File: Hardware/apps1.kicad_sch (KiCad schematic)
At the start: 12 parts, among them U114 TLV9152IDDFR

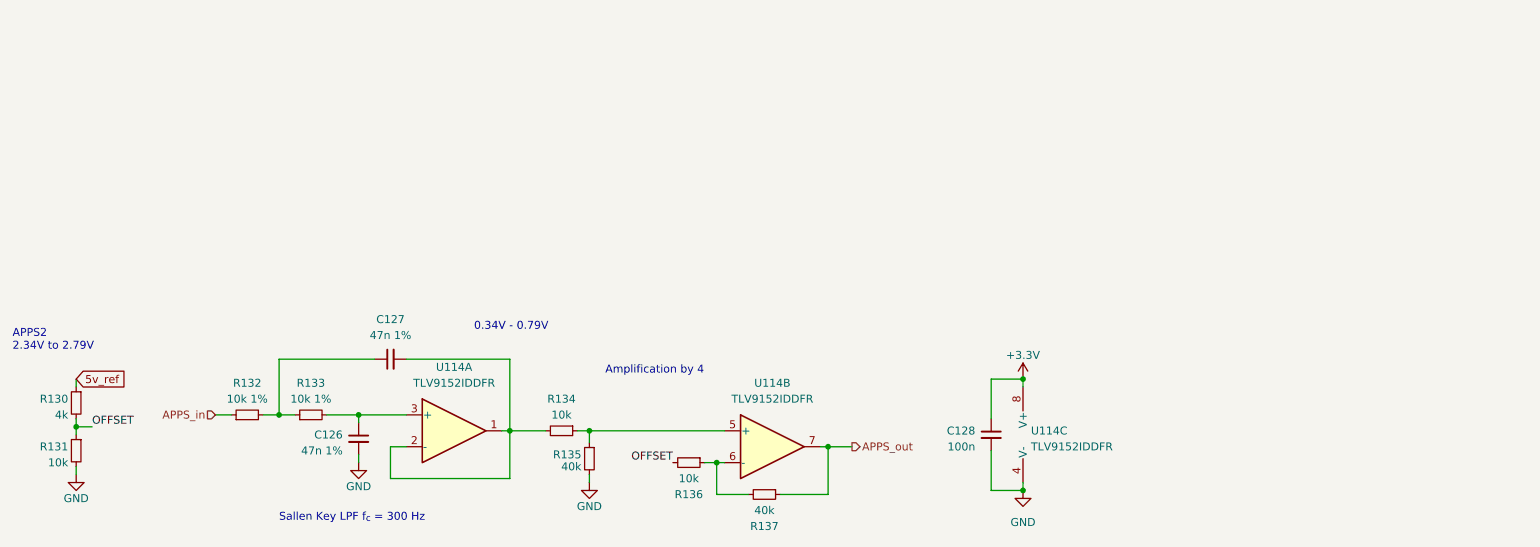
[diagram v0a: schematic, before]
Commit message: Changes in current layout, added tensometers to layout
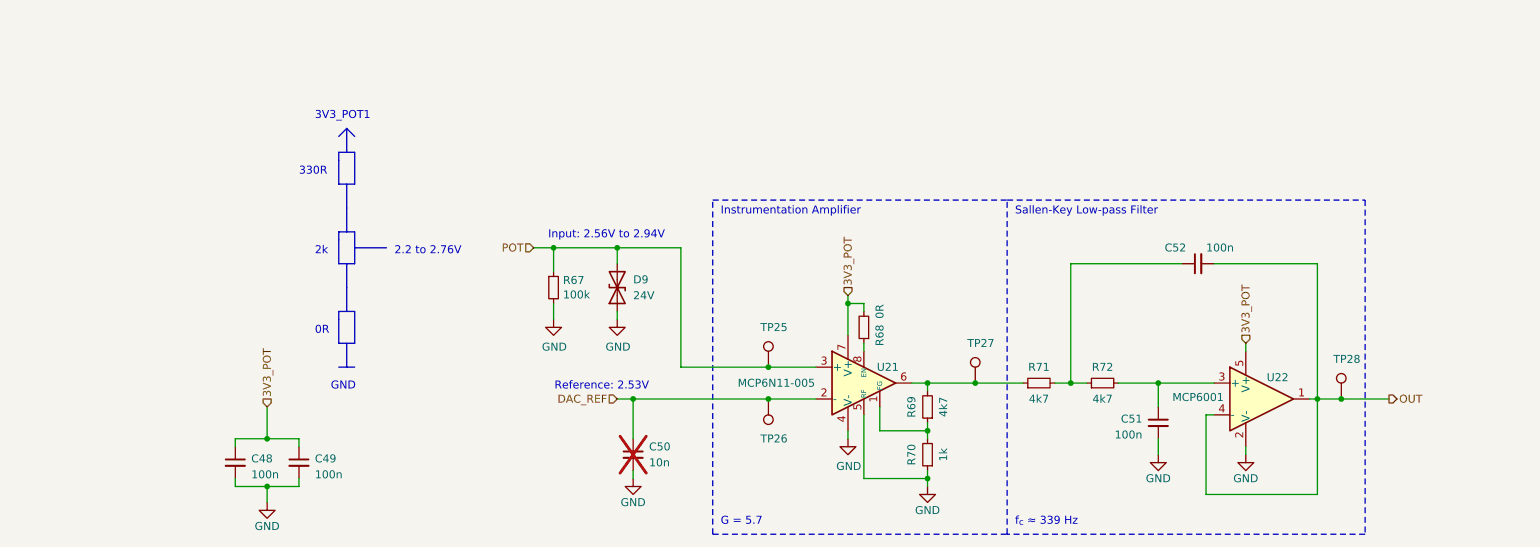
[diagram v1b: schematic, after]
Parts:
- removed C126, C127: 47n 1%, Capacitor_SMD:C_0402_1005Metric_Pad0.74x0.62mm_HandSolder, symbol Device:C_Small
- removed C128: 100n, Capacitor_SMD:C_0402_1005Metric_Pad0.74x0.62mm_HandSolder, symbol Device:C_Small
- removed R130: 4k, Resistor_SMD:R_0402_1005Metric, symbol Device:R_Small
- removed R131, R134, R136: 10k, Resistor_SMD:R_0402_1005Metric, symbol Device:R_Small
- removed R132, R133: 10k 1%, Resistor_SMD:R_0402_1005Metric, symbol Device:R_Small
- removed R135, R137: 40k, Resistor_SMD:R_0402_1005Metric, symbol Device:R_Small
- removed U114: TLV9152IDDFR, Package_TO_SOT_SMD:TSOT-23-8_HandSoldering, symbol Amplifier_Operational:TLV9062
- added C48, C49, C51, C52: 100n, Capacitor_SMD:C_0603_1608Metric_Pad1.08x0.95mm_HandSolder, symbol Device:C_Small
- added C50: 10n, Capacitor_SMD:C_0603_1608Metric_Pad1.08x0.95mm_HandSolder, symbol Device:C_Small
- added D9: 24V, Diode_SMD:D_0603_1608Metric_Pad1.05x0.95mm_HandSolder, symbol Device:D_TVS
- added R67: 100k, Resistor_SMD:R_0603_1608Metric_Pad0.98x0.95mm_HandSolder, symbol Device:R_Small
- added R68: 0R, Resistor_SMD:R_0603_1608Metric_Pad0.98x0.95mm_HandSolder, symbol Device:R_Small
- added R69, R71, R72: 4k7, Resistor_SMD:R_0603_1608Metric_Pad0.98x0.95mm_HandSolder, symbol Device:R_Small
- added R70: 1k, Resistor_SMD:R_0603_1608Metric_Pad0.98x0.95mm_HandSolder, symbol Device:R_Small
- added TP25: APPS_P, TestPoint:TestPoint_Pad_D1.0mm, symbol Connector:TestPoint
- added TP26: APPS_N, TestPoint:TestPoint_Pad_D1.0mm, symbol Connector:TestPoint
- added TP27: APPS_MID, TestPoint:TestPoint_Pad_D1.0mm, symbol Connector:TestPoint
- added TP28: APPS_OUT, TestPoint:TestPoint_Pad_D1.0mm, symbol Connector:TestPoint
- added U21: MCP6N11-005, Package_DFN_QFN:TDFN-8-1EP_3x2mm_P0.5mm_EP1.3x1.4mm, symbol MCP6N11:MCP6N11
- added U22: MCP6001, Package_TO_SOT_SMD:SOT-23-5, symbol Amplifier_Operational:MCP6001-OT
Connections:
- net GND: now also C48.2, C49.2, C50.2, C51.2, D9.1 (A1), R67.2, R70.1, U21.4 (V-), U21.5 (RF), U21.9 (EP), U22.2 (V-)
- new net: R69.1, R70.2, U21.1 (FG)
- new net: R69.2, R71.1, TP27.1, U21.6
- new net: R68.1, U21.8 (EN)
- new net: C52.1, R71.2, R72.1
- new net: C51.1, R72.2, U22.3 (+)
- new net 3V3_POT: C48.1, C49.1, R68.2, U21.7 (V+), U22.5 (V+)
- new net DAC_REF: C50.1, TP26.1, U21.2 (-)
- new net OUT: C52.2, TP28.1, U22.1, U22.4 (-)
- new net POT: D9.2 (A2), R67.1, TP25.1, U21.3 (+)
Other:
- note added: "0R"
- note added: "2.2 to 2.76V"
- note added: "2k"
- note added: "330R"
- note added: "3V3_POT1"
- note added: "G = 5.7"
- note added: "GND"
- note added: "Input: 2.56V to 2.94V"
- note added: "Instrumentation Amplifier"
- note added: "Reference: 2.53V"
- note added: "Sallen-Key Low-pass Filter"
- note added: "f_{c} ≈ 339 Hz"
- note removed: "0.34V - 0.79V"
- note removed: "APPS2 2.34V to 2.79V"
- note removed: "Amplification by 4"
- note removed: "Sallen Key LPF f_{c} = 300 Hz"
- company: Author: Szymon Kostrubiec -> (none)
- title: APPS -> (none)

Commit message: Changes in power section
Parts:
- TP25, TP26, TP27, TP28: footprint TestPoint:TestPoint_Pad_D1.0mm -> TestPoint:TestPoint_THTPad_D1.0mm_Drill0.5mm
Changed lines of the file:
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@@
 			)
 		)
-		(property "Footprint" "TestPoint:TestPoint_Pad_D1.0mm"
+		(property "Footprint" "TestPoint:TestPoint_THTPad_D1.0mm_Drill0.5mm"
 			(at 177.8 96.52 0)
 			(effects
@@
 			)
 		)
-		(property "Footprint" "TestPoint:TestPoint_Pad_D1.0mm"
+		(property "Footprint" "TestPoint:TestPoint_THTPad_D1.0mm_Drill0.5mm"
 			(at 236.22 99.06 0)
 			(effects
@@
 			)
 		)
-		(property "Footprint" "TestPoint:TestPoint_Pad_D1.0mm"
+		(property "Footprint" "TestPoint:TestPoint_THTPad_D1.0mm_Drill0.5mm"
 			(at 134.62 99.06 0)
 			(effects
@@
 			)
 		)
-		(property "Footprint" "TestPoint:TestPoint_Pad_D1.0mm"
+		(property "Footprint" "TestPoint:TestPoint_THTPad_D1.0mm_Drill0.5mm"
 			(at 144.78 93.98 0)
 			(effects

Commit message: sync
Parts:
- renumbered C48 to C43, C49 to C44, C50 to C45, C51 to C46, C52 to C47, D9 to D8, R67 to R61, R68 to R62, R69 to R63, R70 to R64, R71 to R65, R72 to R66, TP25 to TP21, TP26 to TP22, TP27 to TP23, TP28 to TP24, U21 to U19, U22 to U20
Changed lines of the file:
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@@
 (kicad_sch
-	(version 20231120)
+	(version 20250114)
 	(generator "eeschema")
-	(generator_version "8.0")
+	(generator_version "9.0")
 	(paper "A4")
+	(text "330R"
+		(exclude_from_sim no)
+		(at 64.77 63.5 0)
+		(effects
+			(font
+				(size 1.27 1.27)
+			)
+			(justify left bottom)
+		)
+	)
+	(text "Instrumentation Amplifier"
+		(exclude_from_sim no)
+		(at 132.08 69.85 0)
+		(effects
+			(font
+				(size 1.27 1.27)
+			)
+			(justify left bottom)
+		)
+	)
+	(text "Input: 2.56V to 2.94V"
+		(exclude_from_sim no)
+		(at 123.19 73.66 0)
+		(effects
+			(font
+				(size 1.27 1.27)
+			)
+			(justify right bottom)
+		)
+	)
+	(text "0R"
+		(exclude_from_sim no)
+		(at 67.31 88.9 0)
+		(effects
+			(font
+				(size 1.27 1.27)
+			)
+			(justify left bottom)
+		)
+	)
+	(text "2k"
+		(exclude_from_sim no)
+		(at 67.31 76.2 0)
+		(effects
+			(font
+				(size 1.27 1.27)
+			)
+			(justify left bottom)
+		)
+	)
+	(text "Sallen-Key Low-pass Filter"
+		(exclude_from_sim no)
+		(at 179.07 69.85 0)
+		(effects
+			(font
+				(size 1.27 1.27)
+			)
+			(justify left bottom)
+		)
+	)
+	(text "2.2 to 2.76V"
+		(exclude_from_sim no)
+		(at 80.01 76.2 0)
+		(effects
+			(font
+				(size 1.27 1.27)
+			)
+			(justify left bottom)
+		)
+	)
+	(text "Reference: 2.53V"
+		(exclude_from_sim no)
+		(at 120.65 97.79 0)
+		(effects
+			(font
+				(size 1.27 1.27)
+			)
+			(justify right bottom)
+		)
+	)
+	(text "f_{c} ≈ 339 Hz"
+		(exclude_from_sim no)
+		(at 179.07 119.38 0)
+		(effects
+			(font
+				(size 1.27 1.27)
+			)
+			(justify left bottom)
+		)
+	)
+	(text "G = 5.7"
+		(exclude_from_sim no)
+		(at 132.08 119.38 0)
+		(effects
+			(font
+				(size 1.27 1.27)
+			)
+			(justify left bottom)
+		)
+	)
+	(text "3V3_POT1"
+		(exclude_from_sim no)
+		(at 67.31 54.61 0)
+		(effects
+			(font
+				(size 1.27 1.27)
+			)
+			(justify left bottom)
+		)
+	)
+	(text "GND"
+		(exclude_from_sim no)
+		(at 69.85 97.79 0)
+		(effects
+			(font
+				(size 1.27 1.27)
+			)
+			(justify left bottom)
+		)
+	)
 	(junction
 		(at 152.4 83.82)
@@
 		)
 	)
-	(text "330R"
-		(exclude_from_sim no)
-		(at 64.77 63.5 0)
-		(effects
-			(font
-				(size 1.27 1.27)
-			)
-			(justify left bottom)
-		)
-	)
-	(text "Instrumentation Amplifier"
-		(exclude_from_sim no)
-		(at 132.08 69.85 0)
-		(effects
-			(font
-				(size 1.27 1.27)
-			)
-			(justify left bottom)
-		)
-	)
-	(text "Input: 2.56V to 2.94V"
-		(exclude_from_sim no)
-		(at 123.19 73.66 0)
-		(effects
-			(font
-				(size 1.27 1.27)
-			)
-			(justify right bottom)
-		)
-	)
-	(text "0R"
-		(exclude_from_sim no)
-		(at 67.31 88.9 0)
-		(effects
-			(font
-				(size 1.27 1.27)
-			)
-			(justify left bottom)
-		)
-	)
-	(text "2k"
-		(exclude_from_sim no)
-		(at 67.31 76.2 0)
-		(effects
-			(font
-				(size 1.27 1.27)
-			)
-			(justify left bottom)
-		)
-	)
-	(text "Sallen-Key Low-pass Filter"
-		(exclude_from_sim no)
-		(at 179.07 69.85 0)
-		(effects
-			(font
-				(size 1.27 1.27)
-			)
-			(justify left bottom)
-		)
-	)
-	(text "2.2 to 2.76V"
-		(exclude_from_sim no)
-		(at 80.01 76.2 0)
-		(effects
-			(font
-				(size 1.27 1.27)
-			)
-			(justify left bottom)
-		)
-	)
-	(text "Reference: 2.53V"
-		(exclude_from_sim no)
-		(at 120.65 97.79 0)
-		(effects
-			(font
-				(size 1.27 1.27)
-			)
-			(justify right bottom)
-		)
-	)
-	(text "f_{c} ≈ 339 Hz"
-		(exclude_from_sim no)
-		(at 179.07 119.38 0)
-		(effects
-			(font
-				(size 1.27 1.27)
-			)
-			(justify left bottom)
-		)
-	)
-	(text "G = 5.7"
-		(exclude_from_sim no)
-		(at 132.08 119.38 0)
-		(effects
-			(font
-				(size 1.27 1.27)
-			)
-			(justify left bottom)
-		)
-	)
-	(text "3V3_POT1"
-		(exclude_from_sim no)
-		(at 67.31 54.61 0)
-		(effects
-			(font
-				(size 1.27 1.27)
-			)
-			(justify left bottom)
-		)
-	)
-	(text "GND"
-		(exclude_from_sim no)
-		(at 69.85 97.79 0)
-		(effects
-			(font
-				(size 1.27 1.27)
-			)
-			(justify left bottom)
-		)
-	)
 	(hierarchical_label "3V3_POT"
 		(shape input)
 		(at 215.9 90.17 90)
-		(fields_autoplaced yes)
 		(effects
 			(font
@@
 		(shape input)
 		(at 152.4 82.55 90)
-		(fields_autoplaced yes)
 		(effects
 			(font
@@
 		(shape output)
 		(at 238.76 99.06 0)
-		(fields_autoplaced yes)
 		(effects
 			(font
@@
 		(shape input)
 		(at 59.69 100.33 90)
-		(fields_autoplaced yes)
 		(effects
 			(font
@@
 		(shape input)
 		(at 102.235 74.93 180)
-		(fields_autoplaced yes)
 		(effects
 			(font
@@
 		(shape input)
 		(at 115.57 99.06 180)
-		(fields_autoplaced yes)
 		(effects
 			(font
@@
 		(on_board yes)
 		(dnp no)
-		(property "Reference" "U21"
+		(property "Reference" "U19"
 			(at 158.75 93.98 0)
 			(effects
@@
 		(on_board yes)
 		(dnp no)
-		(property "Reference" "R71"
+		(property "Reference" "R65"
 			(at 182.88 93.98 90)
 			(effects
@@
 		(on_board yes)
 		(dnp no)
-		(property "Reference" "C51"
+		(property "Reference" "C46"
 			(at 199.39 102.2413 0)
 			(effects
@@
 		(on_board yes)
 		(dnp no)
-		(property "Reference" "C48"
+		(property "Reference" "C43"
 			(at 57.15 108.5913 0)
 			(effects
@@
 		(on_board yes)
 		(dnp no)
-		(property "Reference" "R72"
+		(property "Reference" "R66"
 			(at 193.04 93.98 90)
 			(effects
@@
 		(on_board yes)
 		(dnp no)
-		(property "Reference" "TP27"
+		(property "Reference" "TP23"
 			(at 171.45 90.17 0)
 			(effects
@@
 		(on_board yes)
 		(dnp no)
-		(property "Reference" "C49"
+		(property "Reference" "C44"
 			(at 67.31 108.5913 0)
 			(effects
@@
 		(on_board yes)
 		(dnp no)
-		(property "Reference" "C52"
+		(property "Reference" "C47"
 			(at 206.3813 74.93 90)
 			(effects
@@
 		(on_board yes)
 		(dnp no)
-		(property "Reference" "R69"
+		(property "Reference" "R63"
 			(at 162.56 100.33 90)
 			(effects
@@
 		(on_board yes)
 		(dnp no)
-		(property "Reference" "U22"
+		(property "Reference" "U20"
 			(at 220.98 95.6311 0)
 			(effects
@@
 		(on_board yes)
 		(dnp no)
-		(property "Reference" "R70"
+		(property "Reference" "R64"
 			(at 162.56 107.95 90)
 			(effects
@@
 		(on_board yes)
 		(dnp no)
-		(property "Reference" "#PWR0151"
+		(property "Reference" "#PWR0143"
 			(at 201.93 114.3 0)
 			(effects
@@
 		(on_board yes)
 		(dnp yes)
-		(property "Reference" "C50"
+		(property "Reference" "C45"
 			(at 120.65 106.68 0)
 			(effects
@@
 		(on_board yes)
 		(dnp no)
-		(property "Reference" "#PWR0145"
+		(property "Reference" "#PWR0137"
 			(at 59.69 121.92 0)
 			(effects
@@
 		(on_board yes)
 		(dnp no)
-		(property "Reference" "R68"
+		(property "Reference" "R62"
 			(at 157.48 88.9 90)
 			(effects
@@
 		(on_board yes)
 		(dnp no)
-		(property "Reference" "#PWR0146"
+		(property "Reference" "#PWR0138"
 			(at 105.41 92.71 0)
 			(effects
@@
 		(on_board yes)
 		(dnp no)
-		(property "Reference" "#PWR0152"
+		(property "Reference" "#PWR0144"
 			(at 215.9 114.3 0)
 			(effects
@@
 		(on_board yes)
 		(dnp no)
-		(property "Reference" "#PWR0148"
+		(property "Reference" "#PWR0140"
 			(at 118.11 118.11 0)
 			(effects
@@
 		(on_board yes)
 		(dnp no)
-		(property "Reference" "#PWR0149"
+		(property "Reference" "#PWR0141"
 			(at 152.4 111.76 0)
 			(effects
@@
 		(dnp no)
 		(fields_autoplaced yes)
-		(property "Reference" "D9"
+		(property "Reference" "D8"
 			(at 118.11 80.01 90)
 			(effects
@@
 		(on_board yes)
 		(dnp no)
-		(property "Reference" "TP28"
+		(property "Reference" "TP24"
 			(at 229.87 92.71 0)
 			(effects
@@
 		(on_board yes)
 		(dnp no)
-		(property "Reference" "R67"
+		(property "Reference" "R61"
 			(at 106.9086 80.1116 0)
 			(effects
@@
 		(on_board yes)
 		(dnp no)
-		(property "Reference" "TP26"
+		(property "Reference" "TP22"
 			(at 138.43 105.41 0)
 			(effects
@@
 		(on_board yes)
 		(dnp no)
-		(property "Reference" "#PWR0147"
+		(property "Reference" "#PWR0139"
 			(at 115.57 92.71 0)
 			(effects
@@
 		(on_board yes)
 		(dnp no)
-		(property "Reference" "#PWR0150"
+		(property "Reference" "#PWR0142"
 			(at 165.1 119.38 0)
 			(effects
@@
 		(on_board yes)
 		(dnp no)
-		(property "Reference" "TP25"
+		(property "Reference" "TP21"
 			(at 138.43 87.63 0)
 			(effects

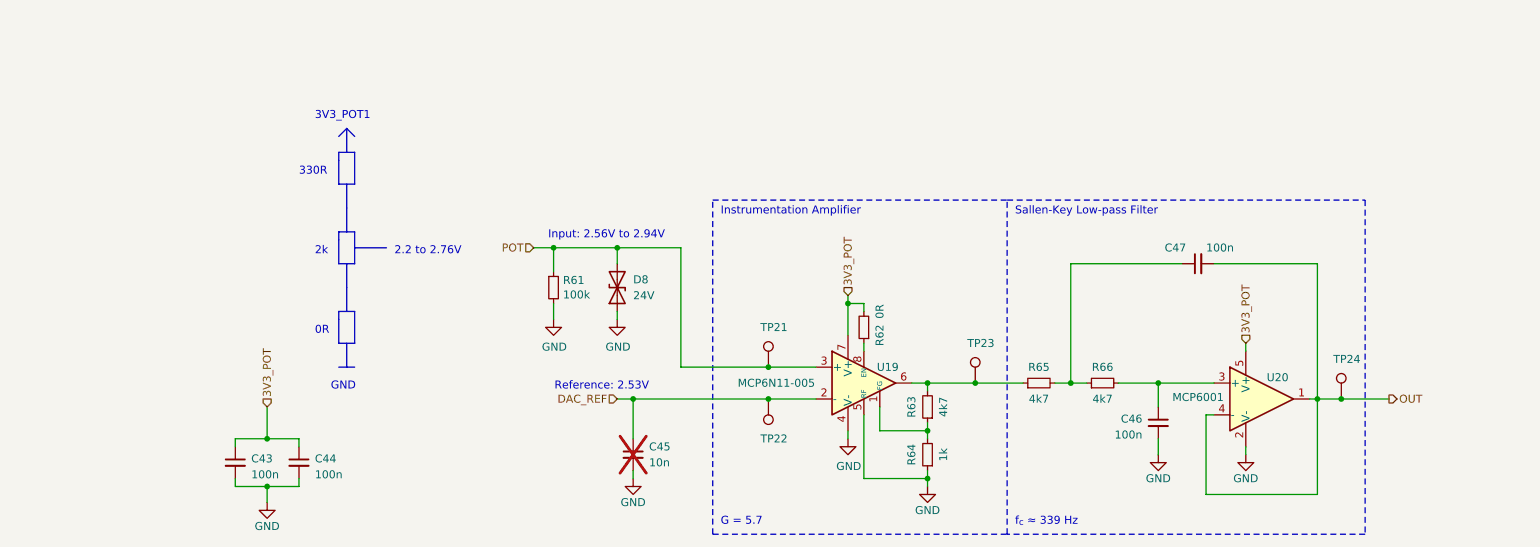
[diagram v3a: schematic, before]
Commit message: Created new hardware version 2.0
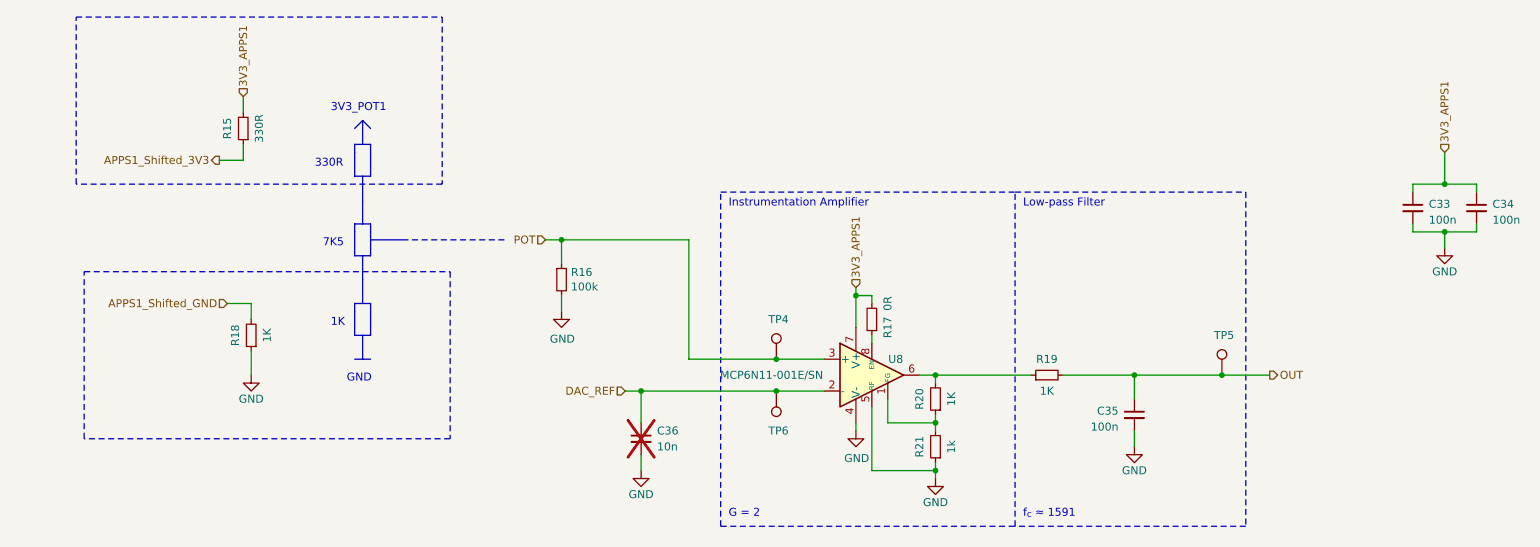
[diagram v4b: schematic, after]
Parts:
- removed C43, C44, C46, C47: 100n, Capacitor_SMD:C_0603_1608Metric_Pad1.08x0.95mm_HandSolder, symbol Device:C_Small
- removed C45: 10n, Capacitor_SMD:C_0603_1608Metric_Pad1.08x0.95mm_HandSolder, symbol Device:C_Small
- removed D8: 24V, Diode_SMD:D_0603_1608Metric_Pad1.05x0.95mm_HandSolder, symbol Device:D_TVS
- removed R61: 100k, Resistor_SMD:R_0603_1608Metric_Pad0.98x0.95mm_HandSolder, symbol Device:R_Small
- removed R62: 0R, Resistor_SMD:R_0603_1608Metric_Pad0.98x0.95mm_HandSolder, symbol Device:R_Small
- removed R63, R65, R66: 4k7, Resistor_SMD:R_0603_1608Metric_Pad0.98x0.95mm_HandSolder, symbol Device:R_Small
- removed R64: 1k, Resistor_SMD:R_0603_1608Metric_Pad0.98x0.95mm_HandSolder, symbol Device:R_Small
- removed TP21: APPS_P, TestPoint:TestPoint_THTPad_D1.0mm_Drill0.5mm, symbol Connector:TestPoint
- removed TP22: APPS_N, TestPoint:TestPoint_THTPad_D1.0mm_Drill0.5mm, symbol Connector:TestPoint
- removed TP23: APPS_MID, TestPoint:TestPoint_THTPad_D1.0mm_Drill0.5mm, symbol Connector:TestPoint
- removed TP24: APPS_OUT, TestPoint:TestPoint_THTPad_D1.0mm_Drill0.5mm, symbol Connector:TestPoint
- removed U19: MCP6N11-005, Package_DFN_QFN:TDFN-8-1EP_3x2mm_P0.5mm_EP1.3x1.4mm, symbol MCP6N11:MCP6N11
- removed U20: MCP6001, Package_TO_SOT_SMD:SOT-23-5, symbol Amplifier_Operational:MCP6001-OT
- added C33, C34, C35: 100n, Capacitor_SMD:C_0603_1608Metric_Pad1.08x0.95mm_HandSolder, symbol Device:C_Small
- added C36: 10n, Capacitor_SMD:C_0603_1608Metric_Pad1.08x0.95mm_HandSolder, symbol Device:C_Small
- added R15: 330R, Resistor_SMD:R_0603_1608Metric_Pad0.98x0.95mm_HandSolder, symbol Device:R_Small
- added R16: 100k, Resistor_SMD:R_0603_1608Metric_Pad0.98x0.95mm_HandSolder, symbol Device:R_Small
- added R17: 0R, Resistor_SMD:R_0603_1608Metric_Pad0.98x0.95mm_HandSolder, symbol Device:R_Small
- added R18, R19, R20: 1K, Resistor_SMD:R_0603_1608Metric_Pad0.98x0.95mm_HandSolder, symbol Device:R_Small
- added R21: 1k, Resistor_SMD:R_0603_1608Metric_Pad0.98x0.95mm_HandSolder, symbol Device:R_Small
- added TP4: APPS_P, TestPoint:TestPoint_THTPad_D1.0mm_Drill0.5mm, symbol Connector:TestPoint
- added TP5: APPS_OUT, TestPoint:TestPoint_THTPad_D1.0mm_Drill0.5mm, symbol Connector:TestPoint
- added TP6: APPS_N, TestPoint:TestPoint_THTPad_D1.0mm_Drill0.5mm, symbol Connector:TestPoint
- added U8: MCP6N11-001E/SN, Package_SO:SOIC-8_3.9x4.9mm_P1.27mm, symbol MCP6N11:MCP6N11
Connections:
- net DAC_REF: now also C36.1, TP6.1, U8.2 (-)
- net GND: now also C33.2, C34.2, C35.2, C36.2, R16.2, R18.1, R21.1, U8.4 (V-), U8.5 (RF)
- net OUT: now also C35.1, R19.2, TP5.1
- net POT: now also R16.1, TP4.1, U8.3 (+)
- new net: R20.1, R21.2, U8.1 (FG)
- new net: R19.1, R20.2, U8.6
- new net: R17.1, U8.8 (EN)
- new net 3V3_APPS1: C33.1, C34.1, R15.2, R17.2, U8.7 (V+)
- new net APPS1_Shifted_3V3: R15.1
- new net APPS1_Shifted_GND: R18.2
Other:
- note added: "1K"
- note added: "7K5"
- note added: "G = 2"
- note added: "Low-pass Filter"
- note added: "f_{c} ≈ 1591"
- note removed: "0R"
- note removed: "2.2 to 2.76V"
- note removed: "2k"
- note removed: "G = 5.7"
- note removed: "Input: 2.56V to 2.94V"
- note removed: "Reference: 2.53V"
- note removed: "Sallen-Key Low-pass Filter"
- note removed: "f_{c} ≈ 339 Hz"
